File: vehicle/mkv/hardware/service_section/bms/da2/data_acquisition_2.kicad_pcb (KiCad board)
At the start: 2 copper layers, 340.1 x 60.8 mm, 72 parts, among them J1 MM_M_VT_12, J2 MM_M_VT_12, J3 MM_M_VT_10, J4 MM_M_VT_12, Q1 BSS308PE, Q11 BSS308PE, Q13 BSS308PE, Q15 BSS308PE, Q3 BSS308PE, Q5 BSS308PE, Q7 BSS308PE, Q9 BSS308PE, T1 Tab_Connect_BMS, T11 Tab_Connect_BMS, T13 Tab_Connect_BMS, T15 Tab_Connect_BMS, T3 Tab_Connect_BMS, T5 Tab_Connect_BMS, T7 Tab_Connect_BMS, T9 Tab_Connect_BMS

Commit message: chore: migrate projects to kicad 6
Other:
- net class Default removed

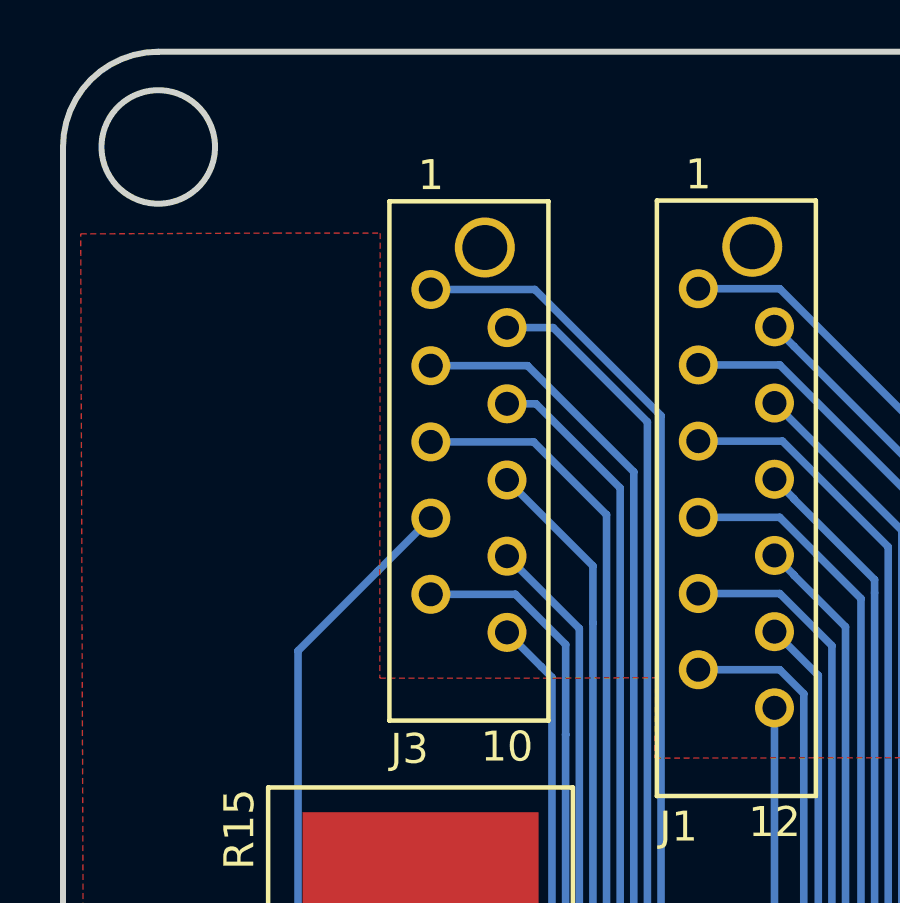
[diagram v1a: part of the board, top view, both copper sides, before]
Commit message: fix: correct 3D model paths where possible
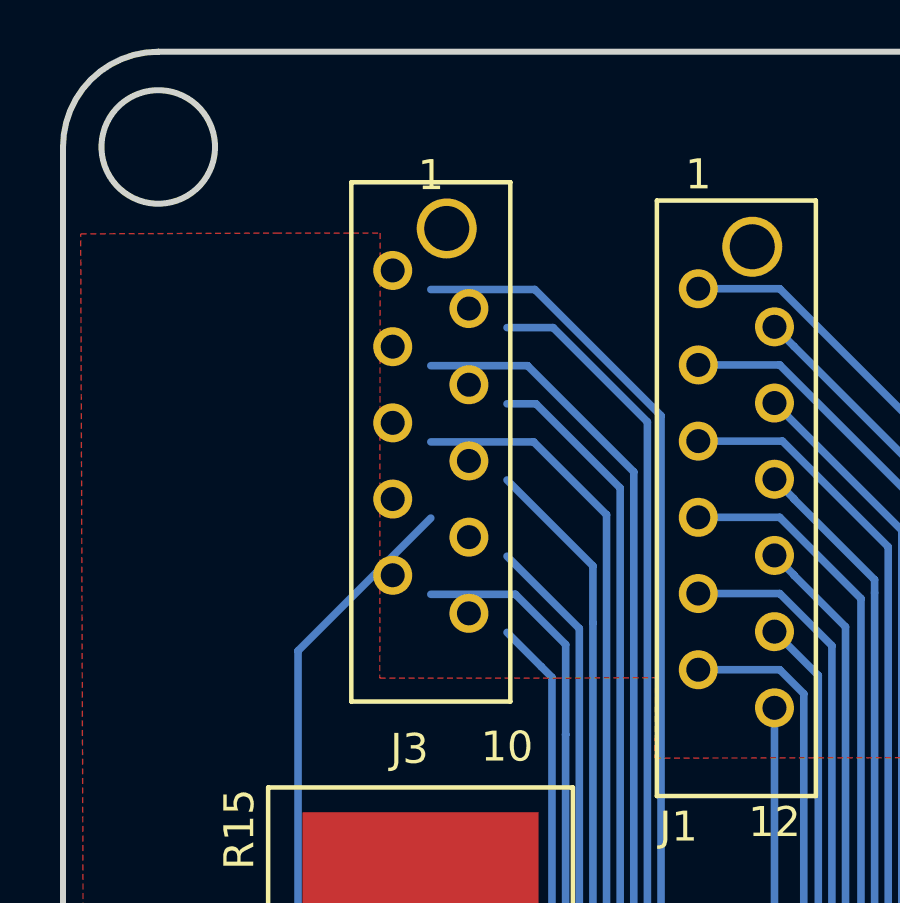
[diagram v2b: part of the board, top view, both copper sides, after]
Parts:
- J1, J2, J4: footprint footprints:micromatch_female_vert_12 -> footprints:micromatch_female_vt_12
